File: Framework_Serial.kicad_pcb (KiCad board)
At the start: 2 copper layers, 26 x 30 mm, 26 parts, among them J1 Conn_01x07_Male, P1 USB_C_Plug_USB2.0, U1 USBLC6-2SC6, U2 CP2102N-A01-GQFN28

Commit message: moved components around: v02
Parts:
- removed VR1: SOT-23_XC6206P332MR, Package_TO_SOT_SMD:SOT-89-3
- added REF**: MountingHole_2.1mm, MountingHole:MountingHole_2.1mm, F.Cu at (72.2, 29.5)
- added REF**: MountingHole_2.1mm, MountingHole:MountingHole_2.1mm, F.Cu at (91.8, 54.2)
- added TP5: P3, TestPoint:TestPoint_Pad_1.5x1.5mm, B.Cu at (88.2, 28.8)
- added TP6: P4, TestPoint:TestPoint_Pad_1.5x1.5mm, B.Cu at (76.8, 28.8)
- added U3: AMS1117-3.3, Package_TO_SOT_SMD:SOT-223-3_TabPin2, F.Cu at (89.5, 40.2)
- C3: value 1u -> 10u; footprint Capacitor_SMD:C_0805_2012Metric -> Capacitor_SMD:C_0603_1608Metric
- C6: footprint Capacitor_SMD:C_0805_2012Metric -> Capacitor_SMD:C_0603_1608Metric
- C7: footprint Capacitor_SMD:C_0603_1608Metric -> Capacitor_SMD:C_0402_1005Metric
- C8: value 1u -> 22u
- R1, R2, R3, R4: footprint Resistor_SMD:R_0805_2012Metric -> Resistor_SMD:R_0402_1005Metric
- TP1: value TestPoint -> CTS; footprint TestPoint:TestPoint_Pad_1.5x1.5mm -> TestPoint:TestPoint_Pad_D1.0mm
- TP2: value TestPoint -> DSR; footprint TestPoint:TestPoint_Pad_1.5x1.5mm -> TestPoint:TestPoint_Pad_D1.0mm; moved to F.Cu
- TP3: value TestPoint -> P1
- TP4: value TestPoint -> P2; moved to F.Cu
- moved TP1 16.3 mm to (76.3, 45.1)
- moved TP2 13.1 mm to (82.7, 40.4), turned to 0 degrees
- moved TP3 11.4 mm to (76.8, 28.8)
- moved C8 8.05 mm to (84.8, 39.8), turned to -90 degrees
- moved C3 7.29 mm to (84.5, 43.0), turned to 90 degrees
- moved R1 6.05 mm to (80.2, 33.8)
- moved C6 5.94 mm to (74.5, 36.0)
- moved U2 5.27 mm to (77.2, 40.8)
- moved R4 4.27 mm to (72.5, 40.5), turned to 0 degrees
- moved R3 3.75 mm to (72.5, 39.5), turned to 180 degrees
- moved C7 3.18 mm to (75.8, 36.5)
- moved U1 1.54 mm to (83.8, 35.5)
- moved R2 1.52 mm to (72.5, 41.5), turned to 0 degrees
- turned TP4 to 0 degrees
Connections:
- J1 pad 3: DTR -> CTS
- P1 pad S1: unconnected-(P1-PadS1) -> GND
- TP1 pad 1: GND -> DTR
- TP2 pad 1: GND -> DSR
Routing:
- net GND: track 25.0 -> 12.7 mm
- net CTS: track 0.00 -> 9.90 mm, vias 0 -> 1
- net Net-(R2-Pad2): track 12.7 -> 3.13 mm
- net Net-(P1-PadA5): track 13.4 -> 4.10 mm, vias 2 -> 0
- net +3V3: track 72.7 -> 64.3 mm, vias 5 -> 10
- net Net-(R3-Pad1): track 9.61 -> 2.92 mm
- net RXD: track 29.4 -> 24.6 mm
- net RTS: track 15.2 -> 10.8 mm
- net ESD_D+: track 3.18 -> 7.45 mm
- net ESD_D-: track 6.93 -> 10.8 mm
- net TXD: track 30.6 -> 26.8 mm
- net DSR: track 0.00 -> 3.36 mm
- net +5V: track 49.6 -> 51.8 mm, vias 2 -> 3
- net DTR: track 12.1 -> 10.6 mm, vias 0 -> 2
- net D+: track 4.46 -> 5.12 mm
- added copper zone on B.Cu, net +3V3
- added copper zone on F.Cu, net +3V3
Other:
- board text added: "CP2102 V02"
- board text added: "DSR"
- board text added: "DTR"
- board text added: "JLCJLCJLCJLC"

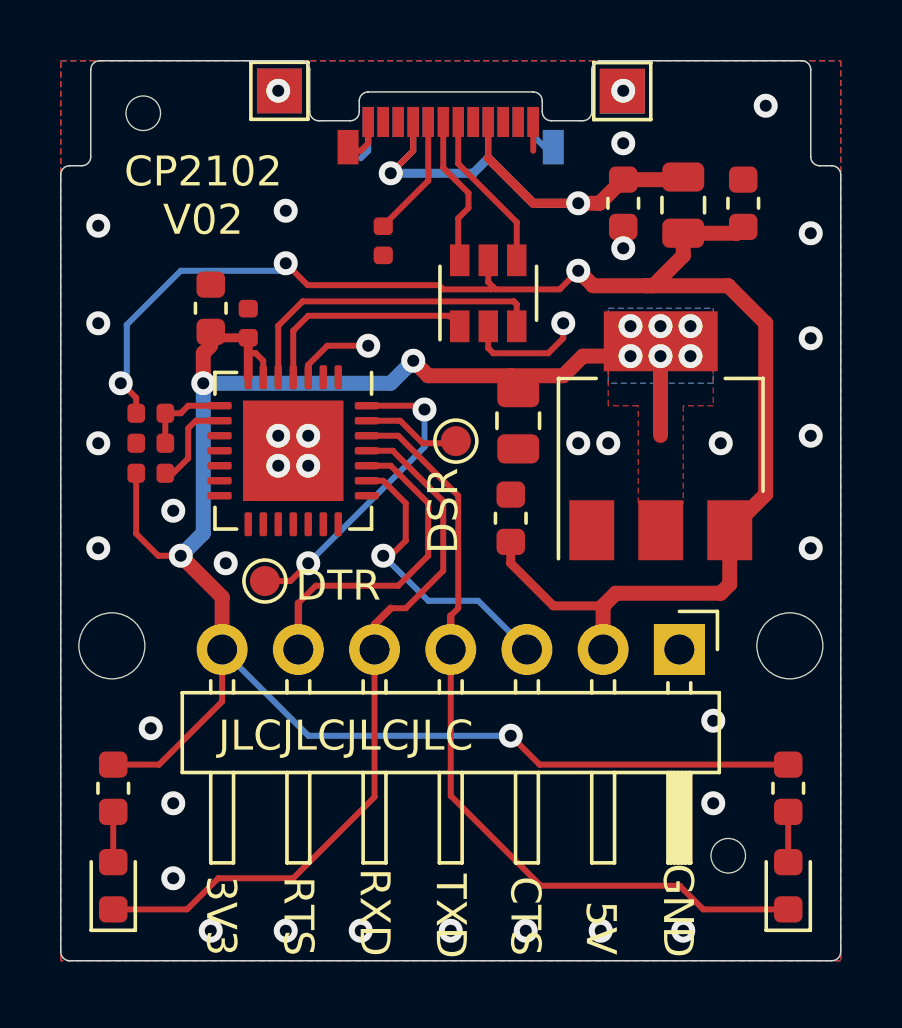
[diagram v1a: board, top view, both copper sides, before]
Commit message: removed unnecessary Vias
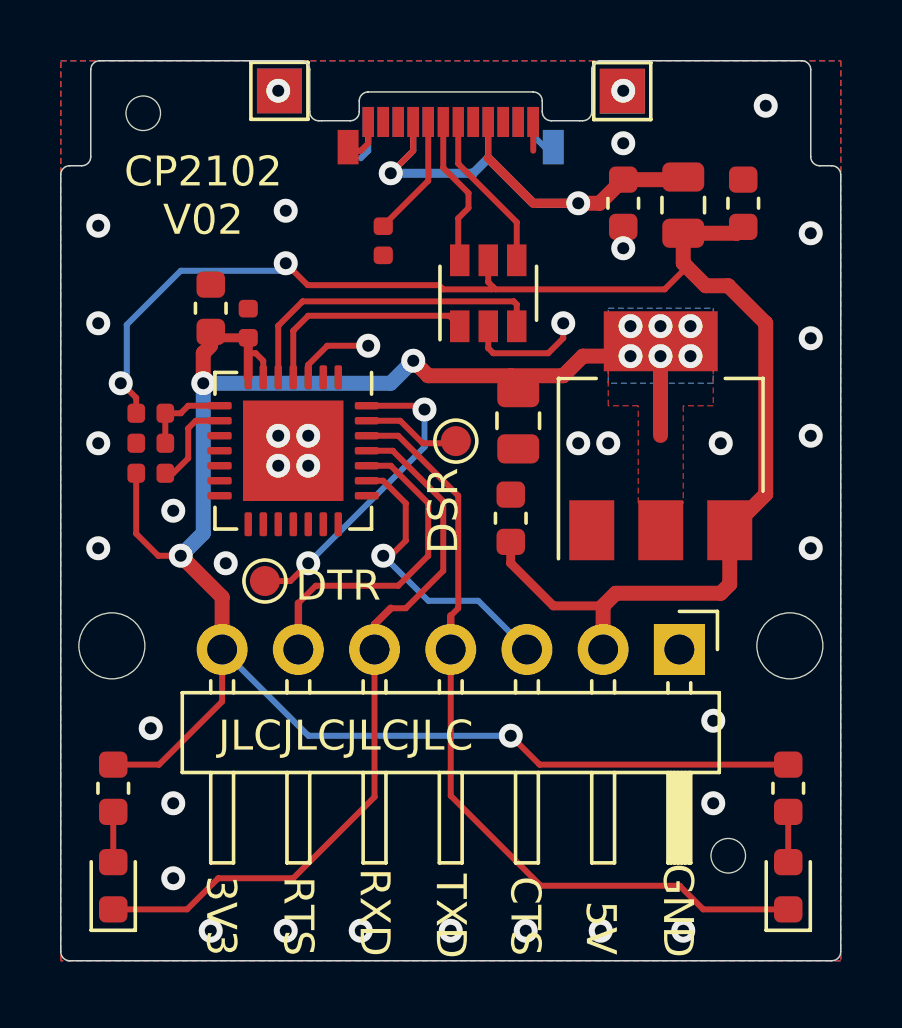
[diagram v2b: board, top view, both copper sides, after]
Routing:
- net +5V: track 51.8 -> 50.7 mm, vias 3 -> 2
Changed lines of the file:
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@@
 (kicad_pcb (version 20210722) (generator pcbnew)
   (general
-    (thickness 1.6)
+    (thickness 0.69)
   )
   (paper "A4")
@@
       (layer "F.Mask" (type "Top Solder Mask") (color "Black") (thickness 0.01) (material "Epoxy") (epsilon_r 3.3) (loss_tangent 0))
       (layer "F.Cu" (type "copper") (thickness 0.035))
-      (layer "dielectric 1" (type "core") (thickness 1.51) (material "FR4") (epsilon_r 4.5) (loss_tangent 0.02))
+      (layer "dielectric 1" (type "core") (thickness 0.6) (material "FR4") (epsilon_r 4.5) (loss_tangent 0.02))
       (layer "B.Cu" (type "copper") (thickness 0.035))
       (layer "B.Mask" (type "Bottom Solder Mask") (color "Black") (thickness 0.01) (material "Epoxy") (epsilon_r 3.3) (loss_tangent 0))
@@
       (drillshape 0)
       (scaleselection 1)
-      (outputdirectory "assembly/")
+      (outputdirectory "gerber/")
     )
   )
@@
       (rotate (xyz 0 0 0))
     )
+    (model "${KIPRJMOD}/1054440001.stp"
+      (offset (xyz 0 3.5 -0.4))
+      (scale (xyz 1 1 1))
+      (rotate (xyz 90 0 0))
+    )
   )
   (footprint "Resistor_SMD:R_0402_1005Metric" (layer "F.Cu")
@@
   (segment (start 79.75 29.79) (end 79.75 30.579022) (width 0.2) (layer "B.Cu") (net 2))
   (segment (start 85.25 29.79) (end 85.25 30.25) (width 0.2) (layer "B.Cu") (net 2))
+  (segment (start 89.629031 35.370969) (end 90.375 34.625) (width 0.2) (layer "F.Cu") (net 3))
   (segment (start 88 45.5) (end 91.5 45.5) (width 0.5) (layer "F.Cu") (net 3))
-  (segment (start 86.129031 35.370969) (end 83.990969 35.370969) (width 0.2) (layer "F.Cu") (net 3))
-  (segment (start 93 42.2) (end 91.8 43.4) (width 0.5) (layer "F.Cu") (net 3))
   (segment (start 91.8 45.2) (end 91.8 43.4) (width 0.5) (layer "F.Cu") (net 3))
   (segment (start 77 34.5) (end 77.729511 35.229511) (width 0.2) (layer "F.Cu") (net 3))
-  (segment (start 89 35.25) (end 91.75 35.25) (width 0.5) (layer "F.Cu") (net 3))
-  (segment (start 89 35.25) (end 89.25 35.25) (width 0.5) (layer "F.Cu") (net 3))
-  (segment (start 86.75 34.75) (end 87.25 35.25) (width 0.5) (layer "F.Cu") (net 3))
   (segment (start 84.5 43.7875) (end 84.5 44.5) (width 0.3) (layer "F.Cu") (net 3))
-  (segment (start 83.990969 35.370969) (end 83.935 35.315) (width 0.2) (layer "F.Cu") (net 3))
+  (segment (start 83.990969 35.370969) (end 89.629031 35.370969) (width 0.2) (layer "F.Cu") (net 3))
   (segment (start 87.58 47.375) (end 87.58 45.92) (width 0.5) (layer "F.Cu") (net 3))
   (segment (start 87.58 45.92) (end 88 45.5) (width 0.5) (layer "F.Cu") (net 3))
-  (segment (start 89.25 35.25) (end 90.25 34.25) (width 0.5) (layer "F.Cu") (net 3))
   (segment (start 85.92 45.92) (end 87.58 45.92) (width 0.3) (layer "F.Cu") (net 3))
-  (segment (start 93 36.5) (end 93 42.2) (width 0.5) (layer "F.Cu") (net 3))
   (segment (start 72.015 38.985) (end 72.015 39.5) (width 0.2) (layer "F.Cu") (net 3))
+  (segment (start 90.25 34.5) (end 90.25 33.5) (width 0.5) (layer "F.Cu") (net 3))
   (segment (start 82.25 35.370969) (end 83.879031 35.370969) (width 0.2) (layer "F.Cu") (net 3))
-  (segment (start 87.25 35.25) (end 89 35.25) (width 0.5) (layer "F.Cu") (net 3))
+  (segment (start 93 42.2) (end 93 36.5) (width 0.5) (layer "F.Cu") (net 3))
   (segment (start 71.5 38.5) (end 71.53 38.5) (width 0.2) (layer "F.Cu") (net 3))
   (segment (start 77.729511 35.229511) (end 82.108542 35.229511) (width 0.2) (layer "F.Cu") (net 3))
-  (segment (start 86.75 34.75) (end 86.129031 35.370969) (width 0.2) (layer "F.Cu") (net 3))
+  (segment (start 91 35.25) (end 90.375 34.625) (width 0.5) (layer "F.Cu") (net 3))
   (segment (start 91.5 45.5) (end 91.8 45.2) (width 0.5) (layer "F.Cu") (net 3))
   (segment (start 84.5 44.5) (end 85.92 45.92) (width 0.3) (layer "F.Cu") (net 3))
-  (segment (start 90.25 34.25) (end 90.25 33.5) (width 0.5) (layer "F.Cu") (net 3))
+  (segment (start 90.375 34.625) (end 90.25 34.5) (width 0.5) (layer "F.Cu") (net 3))
+  (segment (start 91.8 43.4) (end 93 42.2) (width 0.5) (layer "F.Cu") (net 3))
+  (segment (start 93 36.5) (end 91.75 35.25) (width 0.5) (layer "F.Cu") (net 3))
   (segment (start 83.75 35.13) (end 83.75 34.4) (width 0.2) (layer "F.Cu") (net 3))
   (segment (start 71.53 38.5) (end 72.015 38.985) (width 0.2) (layer "F.Cu") (net 3))
@@
   (segment (start 83.879031 35.370969) (end 83.935 35.315) (width 0.2) (layer "F.Cu") (net 3))
   (segment (start 82.108542 35.229511) (end 82.25 35.370969) (width 0.2) (layer "F.Cu") (net 3))
+  (segment (start 91.75 35.25) (end 91 35.25) (width 0.5) (layer "F.Cu") (net 3))
+  (segment (start 83.935 35.315) (end 83.990969 35.370969) (width 0.2) (layer "F.Cu") (net 3))
   (segment (start 92.0375 33.5) (end 92.25 33.2875) (width 0.5) (layer "F.Cu") (net 3))
-  (segment (start 91.75 35.25) (end 93 36.5) (width 0.5) (layer "F.Cu") (net 3))
   (via (at 71.5 38.5) (size 0.8) (drill 0.4) (layers "F.Cu" "B.Cu") (net 3))
   (via (at 77 34.5) (size 0.8) (drill 0.4) (layers "F.Cu" "B.Cu") (net 3))
-  (via (at 86.75 34.75) (size 0.8) (drill 0.4) (layers "F.Cu" "B.Cu") (net 3))
   (segment (start 77 34.5) (end 76.75 34.75) (width 0.2) (layer "B.Cu") (net 3))
   (segment (start 73.5 34.75) (end 71.699511 36.550489) (width 0.2) (layer "B.Cu") (net 3))
